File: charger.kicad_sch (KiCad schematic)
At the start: 19 parts, among them U1_CHARGER1 IP2326

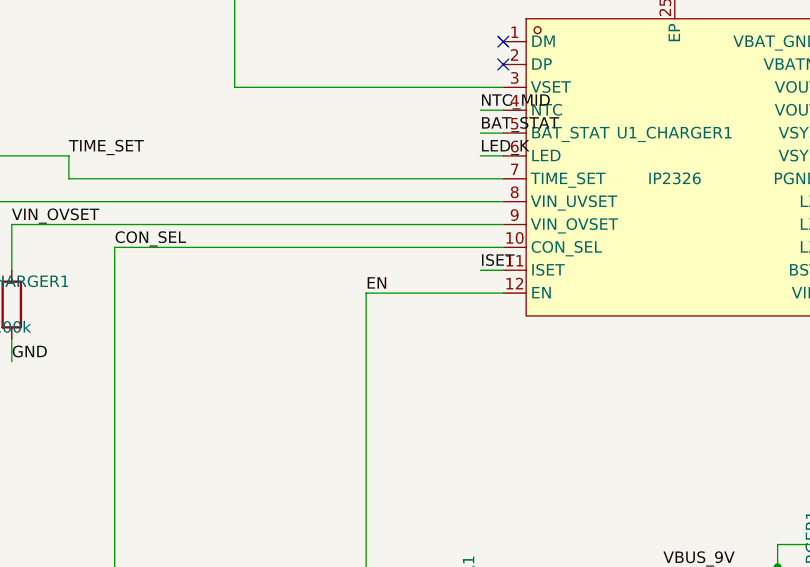
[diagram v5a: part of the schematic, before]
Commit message: Fix EN cross-sheet collision + tag charger VSYS/BAT decoupling caps
EN was accidentally shared across charger and buckboost

Both sheets carried a local label named "EN" — kicad-cli sch export
netlist correctly namespaces these as /charger/EN and /buckboost/EN, but
the .kicad_pcb had ONE net "EN" (net 42) with all four pads collapsed
into it: IP2326 pin 11 was electrically tied to LM5176 pin 1 through PCB
copper.  IP2326.EN is pulled up to VBUS_9V via R9_CHARGER1 (9V rail),
LM5176.EN is pulled up to BAT+ via R6_BUCKBOOST1 (12V rail); shorting
them would fight the pull-ups and give indeterminate enable behaviour.

Renamed the labels to make them unambiguously distinct:

  charger:   EN → CHG_EN
  buckboost: EN → BB_EN

Post-sync verification:
  EN     — 0 pads
  CHG_EN — R9_CHARGER1.2, U1_CHARGER1.11
  BB_EN  — R6_BUCKBOOST1.1, U1_BUCKBOOST1.1

Underlying sync_schematic_to_board bug (collapsing same-named local
labels across sheets when the kicad-cli netlist keeps them separate) is
filed for follow-up on the MCP-server side.  Sweep for other cross-sheet
collisions: only VBUS_9V (input↔charger, intentional) was found.

C2/C3/C4_CHARGER1 decoupling tags added

The earlier decoupling analyser only spotted caps whose non-power pad
lands on a *single* IC pin AND whose ground pad is literal "GND".  It
missed:

  C2_CHARGER1 (22uF) — VSYS bulk cap → tag DECOUPLING to U1_CHARGER1.19
  C3_CHARGER1 (22uF) — VSYS bulk cap → tag DECOUPLING to U1_CHARGER1.20
  C4_CHARGER1 (10uF) — BAT+ input cap → tag DECOUPLING to U1_CHARGER1.21

Distributes across VSYS pins 19+20 so the two 22uF caps don't fight for
the same target pin.  C4 was floating in the last relax pass because its
BAT+ pad was PLANE-classified (via META1 singleton) and GND is a
44-node auto-PLANE; explicit DECOUPLING gives it a target to anchor to.

Co-Authored-By: Claude Opus 4.7 <noreply@anthropic.com>
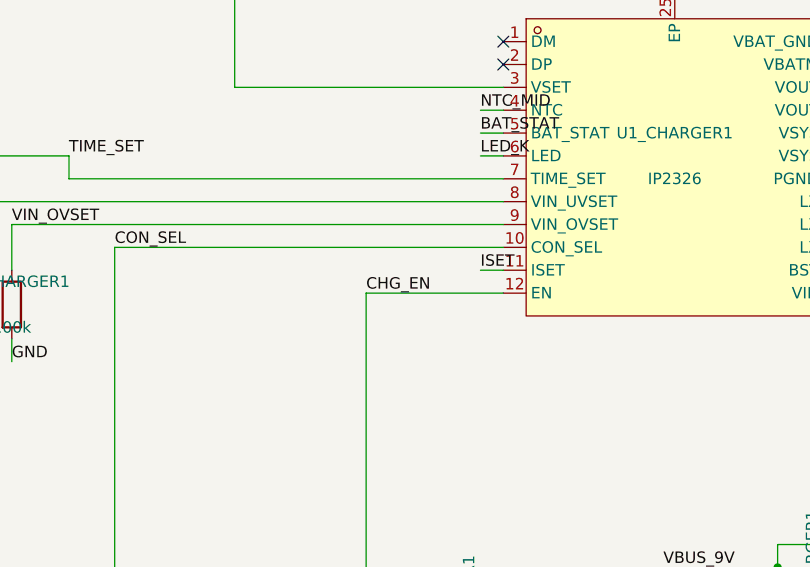
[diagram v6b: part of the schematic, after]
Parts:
- C2_CHARGER1: Pin_Spring_Class:1 (none) -> {"U1_CHARGER1.19":"DECOUPLING"}
- C3_CHARGER1: Pin_Spring_Class:1 (none) -> {"U1_CHARGER1.20":"DECOUPLING"}
- C4_CHARGER1: Pin_Spring_Class:1 (none) -> {"U1_CHARGER1.21":"DECOUPLING"}
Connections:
- net EN renamed CHG_EN
